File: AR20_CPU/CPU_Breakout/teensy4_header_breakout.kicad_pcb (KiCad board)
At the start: 4 copper layers, 65 x 77 mm, 80 parts, among them SW1 SW_SPST, U2 MCP1700_SOT23

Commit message: E
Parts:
- C11: value 100u -> .1u
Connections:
- net 25_A11 renamed 25_RX6_A11
- net 8_IN1 renamed 8_TX2_IN1
- CANmodule1 pad 1: 22_CTX1 -> 31_CTX3
- CANmodule1 pad 4: 23_CRX1 -> 30_CRX3
- D9 pad 1: 24_A10 -> 26_A12
- MX1 pad 22: 24_A10 -> 24_TX6_A10
- MX1 pad 37: 31_CTX3 -> 21_RX5
- MX1 pad 39: 30_CRX3 -> 20_TX5
- MX1 pad 43: 26_A12 -> Ground
- OpAmp1 pad 3: 24_A10 -> 26_A12
- OpAmp1 pad 4: 24_A10 -> 26_A12
- Teensy4.0 pad 10: 22_CTX1 -> Out1
- Teensy4.0 pad 12: Out2 -> 21_RX5
- Teensy4.0 pad 14: Out1 -> 20_TX5
- Teensy4.0 pad 38: 24_A10 -> 24_TX6_A10
- Teensy4.0 pad 8: 23_CRX1 -> Out2
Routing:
- net 24_A10: track 66.8 -> 0.00 mm, vias 2 -> 0
- net 23_CRX1: track 53.3 -> 0.00 mm, vias 1 -> 0
- net 24_TX6_A10: track 0.00 -> 49.8 mm
- net 22_CTX1: track 46.5 -> 0.00 mm, vias 1 -> 0
- net 20_TX5: track 0.00 -> 33.9 mm, vias 0 -> 2
- net 21_RX5: track 0.00 -> 27.8 mm, vias 0 -> 2
- net 31_CTX3: track 27.6 -> 17.6 mm, vias 0 -> 1
- net Out2: track 17.9 -> 15.9 mm
- net 26_A12: track 43.3 -> 41.5 mm, vias 0 -> 2
- net Out1: track 25.0 -> 23.2 mm
- net 30_CRX3: track 23.3 -> 21.5 mm, vias 0 -> 2
- net 12V_IN: track 71.4 -> 72.1 mm

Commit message: E2
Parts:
- removed C12: 0.1u, Capacitor_SMD:C_0603_1608Metric
- removed C13: 1u, Capacitor_SMD:C_0603_1608Metric
- removed JP11, JP12: SolderJumper_2_Open, Jumper:SolderJumper-2_P1.3mm_Open_RoundedPad1.0x1.5mm
- removed U2: MCP1700_SOT23, Package_TO_SOT_SMD:SOT-23
- moved JP10 5.95 mm to (129.7, 88.1), turned to 0 degrees
- moved R21 2.53 mm to (130.4, 90.3), turned to 0 degrees
- moved R22 2.45 mm to (130.4, 92.0), turned to 180 degrees
- moved C19 2.42 mm to (130.5, 94.0), turned to 180 degrees
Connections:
- C19 pad 1: Net-(C19-Pad1) -> IN+
- JP10 pad 1: IN+ -> Net-(JP10-Pad1)
- JP10 pad 2: Net-(C19-Pad1) -> VBAT
- MX1 pad 20: 3.3V -> Ground
- MX1 pad 21: 3V3 -> 3.3V
- R21 pad 1: VBAT -> Net-(JP10-Pad1)
- R21 pad 2: Net-(C19-Pad1) -> IN+
- R22 pad 1: Net-(C19-Pad1) -> IN+
- SDcard1 pad 4: Net-(JP11-Pad1) -> 3.3V
- Teensy4.0 pad 30: 3V3 -> 3.3V
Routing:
- net Net-(JP11-Pad1): track 25.3 -> 0.00 mm
- net 3V3: track 25.3 -> 0.00 mm
- net Net-(C19-Pad1): track 6.73 -> 0.00 mm
- net Vinn_5V: track 154.5 -> 148.2 mm
- net 3V3_OUT: track 5.73 -> 0.00 mm, vias 1 -> 0
- net IN+: track 5.58 -> 9.22 mm
- net Net-(JP10-Pad1): track 0.00 -> 3.30 mm
- net 3.3V: track 46.5 -> 45.0 mm, vias 1 -> 2
- added copper zone on Back_2_3V3, net 3.3V
- removed copper zone on Back_2_3V3, net 3V3_OUT

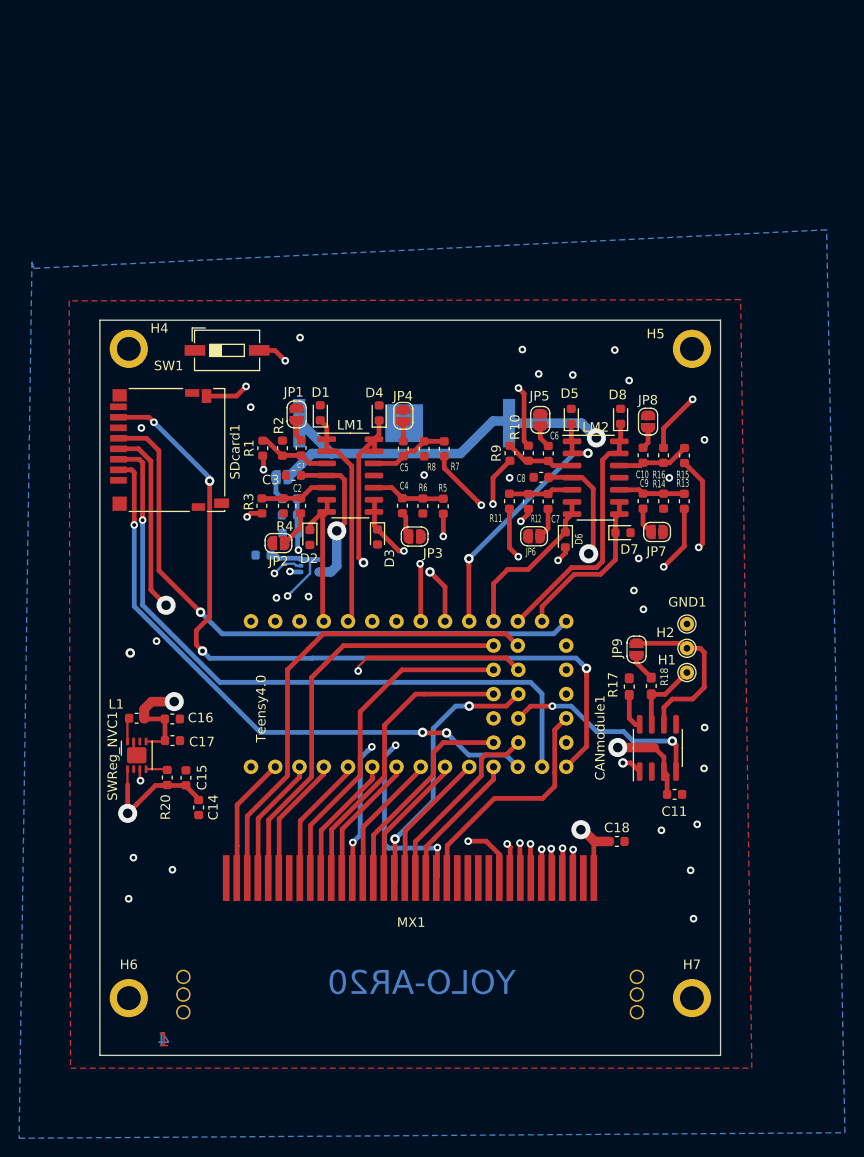
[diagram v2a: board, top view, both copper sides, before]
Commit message: Fixed push button
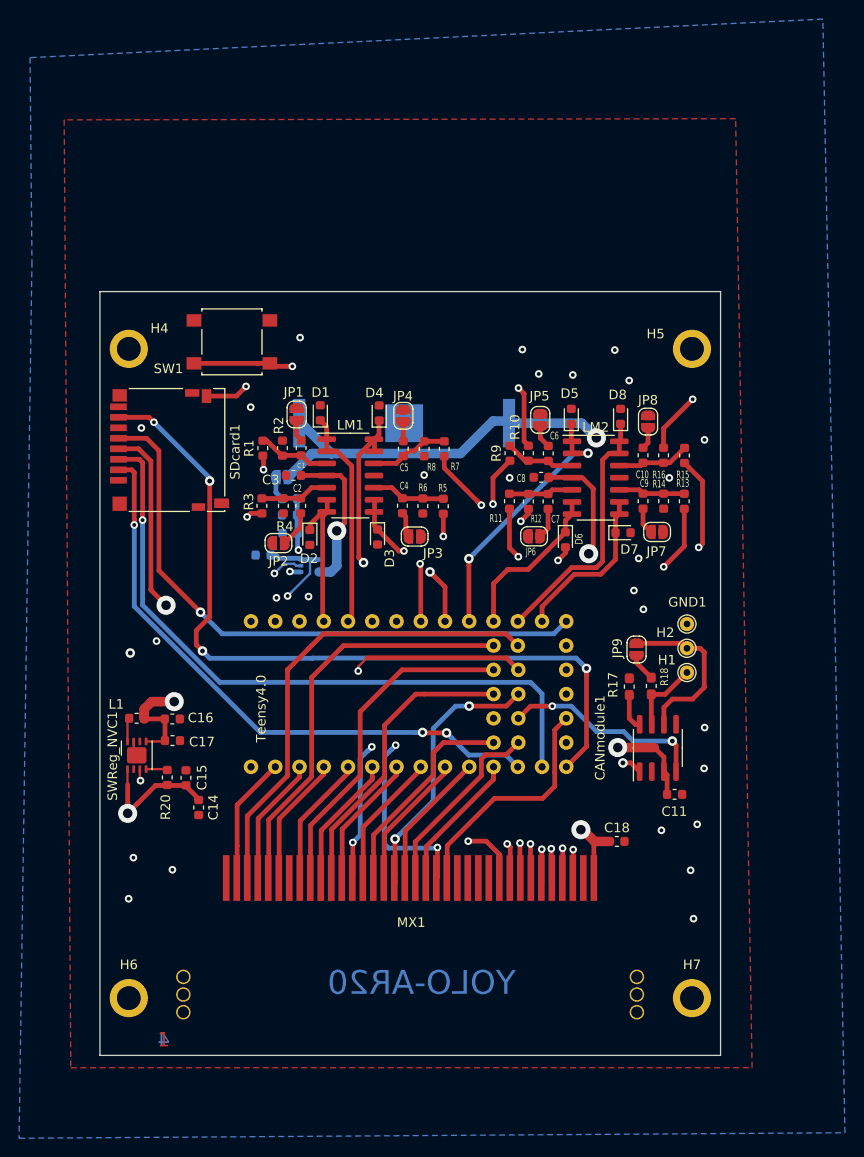
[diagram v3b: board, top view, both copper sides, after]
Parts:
- SW1: value SW_SPST -> SW_Push_Dual; footprint Button_Switch_SMD:SW_DIP_SPSTx01_Slide_6.7x4.1mm_W6.73mm_P2.54mm_LowProfile_JPin -> Button_Switch_SMD:SW_SPST_B3S-1000
- moved SW1 1.03 mm to (124.4, 73.9)
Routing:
- net ON_OFF: track 59.7 -> 66.0 mm
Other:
- board size 65 x 77 mm -> 65 x 80 mm

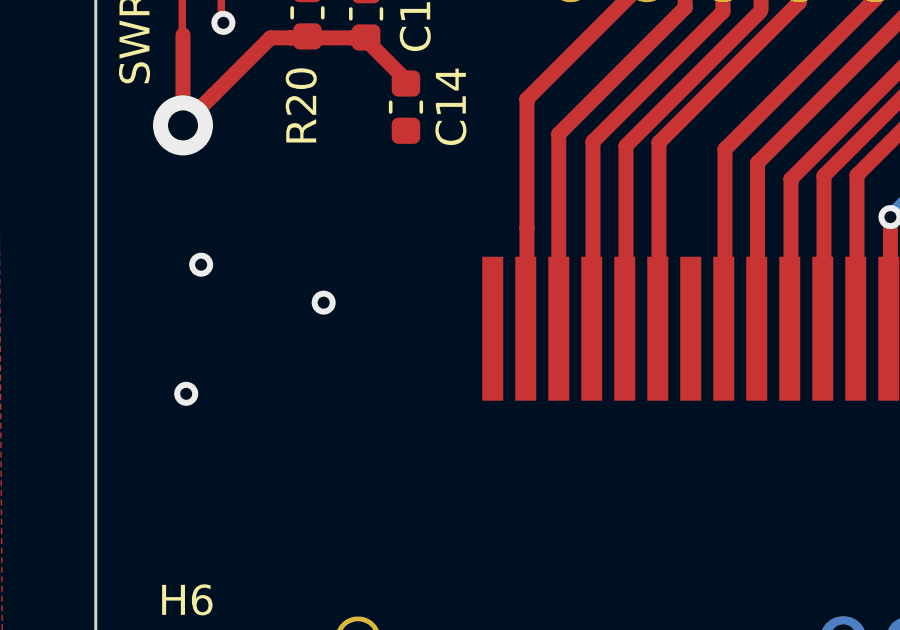
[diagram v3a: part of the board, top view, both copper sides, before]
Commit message: Added 5V pin
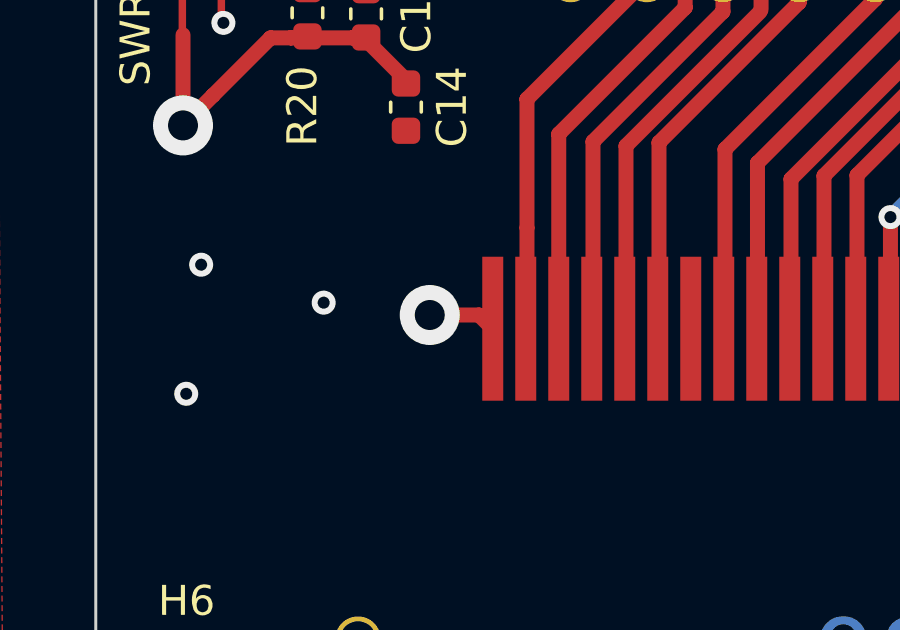
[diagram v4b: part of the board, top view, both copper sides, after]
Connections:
- MX1 pad 20: Ground -> Vinn_5V
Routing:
- net Vinn_5V: track 148.2 -> 150.7 mm, vias 4 -> 5
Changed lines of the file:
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@@
     (thickness 1.6)
     (drawings 9)
-    (tracks 695)
+    (tracks 699)
     (zones 0)
     (modules 75)
@@
     (add_net "Net-(CANmodule1-Pad7)")
     (add_net "Net-(CANmodule1-Pad8)")
+    (add_net "Net-(IC1-Pad1)")
+    (add_net "Net-(IC1-Pad10)")
+    (add_net "Net-(IC1-Pad11)")
+    (add_net "Net-(IC1-Pad12)")
+    (add_net "Net-(IC1-Pad13)")
+    (add_net "Net-(IC1-Pad14)")
+    (add_net "Net-(IC1-Pad2)")
+    (add_net "Net-(IC1-Pad3)")
+    (add_net "Net-(IC1-Pad4)")
+    (add_net "Net-(IC1-Pad5)")
+    (add_net "Net-(IC1-Pad6)")
+    (add_net "Net-(IC1-Pad7)")
+    (add_net "Net-(IC1-Pad8)")
+    (add_net "Net-(IC1-Pad9)")
     (add_net "Net-(JP10-Pad1)")
     (add_net "Net-(JP9-Pad1)")
@@
     (pad 60 thru_hole circle (at -23.75 -0.23642) (size 1.524 1.524) (drill 1.2) (layers *.Cu *.Mask))
     (pad 20 smd rect (at -19.25828 -10.58926) (size 0.7 4.8) (layers Front_GND F.Paste F.Mask)
-      (net 1 Ground))
+      (net 4 Vinn_5V))
     (pad 1 smd rect (at -18.15828 -10.58926) (size 0.7 4.8) (layers Front_GND F.Paste F.Mask)
       (net 34 0_RX1))
@@
   (segment (start 114.10454 116.88838) (end 114.42954 117.21338) (width 0.25) (layer Front_GND) (net 1))
   (segment (start 114.10454 115.76338) (end 114.10454 116.88838) (width 0.25) (layer Front_GND) (net 1))
-  (segment (start 123.8258 130.51616) (end 123.84278 130.53314) (width 0.5) (layer Front_GND) (net 1))
+  (via (at 121.70156 129.61112) (size 2) (drill 1) (layers Front_GND Back_GND) (net 4))
+  (segment (start 123.8258 130.51616) (end 123.84278 130.53314) (width 0.5) (layer Front_GND) (net 4))
   (segment (start 151.75 82.2) (end 148.34438 85.60562) (width 1) (layer Back_GND) (net 2))
   (segment (start 153.385 82.2) (end 151.75 82.2) (width 1) (layer Back_GND) (net 2))
@@
   (segment (start 115.9891 111.58982) (end 116.939627 111.58982) (width 1) (layer Front_GND) (net 4))
   (segment (start 115.20678 112.3569) (end 115.20678 112.37214) (width 0.5) (layer Front_GND) (net 4))
+  (segment (start 123.67768 129.94438) (end 123.80162 130.06832) (width 0.5) (layer Front_GND) (net 4))
+  (segment (start 123.34442 129.61112) (end 123.80162 130.06832) (width 0.5) (layer Front_GND) (net 4))
+  (segment (start 121.70156 129.61112) (end 123.34442 129.61112) (width 0.5) (layer Front_GND) (net 4))
   (via (at 121.113209 102.22507) (size 1) (drill 0.5) (layers Front_GND Back_GND) (net 5))
   (segment (start 123.376138 104.487999) (end 158.109901 104.487999) (width 0.5) (layer Back_GND) (net 5))

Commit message: Edit pads
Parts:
- GND1, H1, H2: footprint TestPoint:TestPoint_THTPad_D1.5mm_Drill0.7mm -> TestPoint:TestPoint_THTPad_D2.0mm_Drill1.0mm
- moved GND1 1.37 mm to (172.2, 102.1)
- moved H2 0.62 mm to (172.2, 105.4)
- moved Teensy4.0 0.20 mm to (126.6, 118.4)
- moved H1 0.10 mm to (172.2, 108.5)
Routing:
- net Net-(CANmodule1-Pad6): track 18.0 -> 18.7 mm

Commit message: Edit pads and traces
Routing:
- net VBAT: track 74.2 -> 75.1 mm
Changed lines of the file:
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@@
   (page A4)
   (layers
-    (0 Front_GND signal hide)
-    (1 Front_2_5V signal hide)
+    (0 Front_GND signal)
+    (1 Front_2_5V signal)
     (2 Back_2_3V3 signal)
-    (31 Back_GND signal hide)
+    (31 Back_GND signal)
     (32 B.Adhes user)
     (33 F.Adhes user)
@@
   (segment (start 148.34438 85.60562) (end 135.88746 85.60562) (width 1) (layer Back_GND) (net 2))
   (via (at 162.57016 83.9724) (size 2) (drill 1) (layers Front_GND Back_GND) (net 2))
-  (segment (start 163.570159 111.709841) (end 159.42 115.86) (width 1) (layer Back_2_3V3) (net 2))
-  (segment (start 162.57016 83.9724) (end 163.570159 84.972399) (width 1) (layer Back_2_3V3) (net 2))
-  (segment (start 163.570159 84.972399) (end 163.570159 111.709841) (width 1) (layer Back_2_3V3) (net 2))
   (segment (start 161.570161 82.972401) (end 162.57016 83.9724) (width 1) (layer Back_GND) (net 2))
   (segment (start 153.42058 82.42808) (end 161.02584 82.42808) (width 1) (layer Back_GND) (net 2))
@@
   (segment (start 132.77342 85.60562) (end 130.302 88.07704) (width 1) (layer Back_GND) (net 2))
   (segment (start 134.82062 85.60562) (end 132.77342 85.60562) (width 1) (layer Back_GND) (net 2))
+  (segment (start 164.65042 110.62958) (end 159.42 115.86) (width 1) (layer Back_2_3V3) (net 2))
+  (segment (start 162.57016 83.9724) (end 164.65042 86.05266) (width 1) (layer Back_2_3V3) (net 2))
+  (segment (start 164.65042 86.05266) (end 164.65042 110.62958) (width 1) (layer Back_2_3V3) (net 2))
   (via (at 132.42036 100.58908) (size 0.8) (drill 0.4) (layers Front_GND Back_GND) (net 3))
   (via (at 130.72618 76.4794) (size 0.8) (drill 0.4) (layers Front_GND Back_GND) (net 3))

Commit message: Gerber file 1.0 generated
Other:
- board text added: "T4.0AR20"
- board text removed: "YOLO-AR20"
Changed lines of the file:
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@@
     (effects (font (size 1.5 1.5) (thickness 0.3)))
   )
-  (gr_text YOLO-AR20 (at 144.26184 141.04112) (layer Back_GND)
+  (gr_text T4.0AR20 (at 144.26184 141.04112) (layer Back_GND)
     (effects (font (size 2.5 2.5) (thickness 0.625)) (justify mirror))
   )

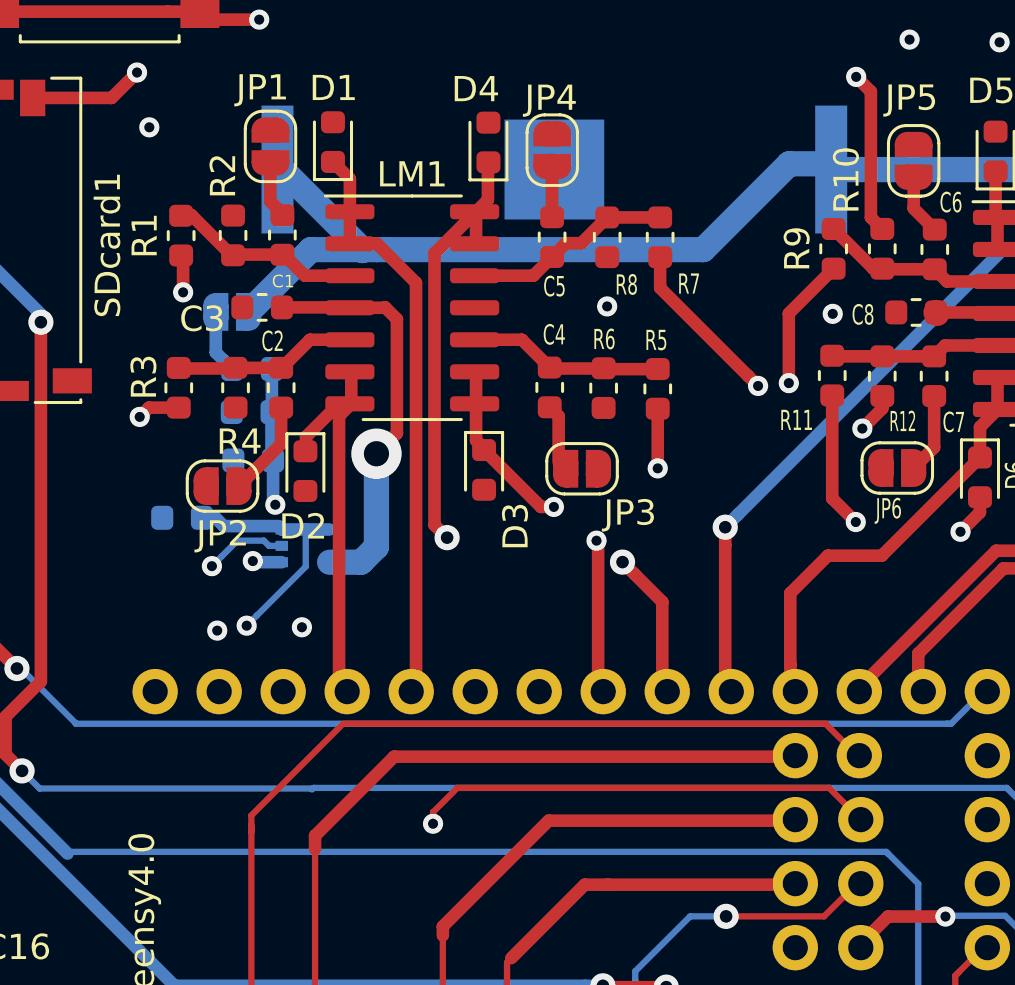
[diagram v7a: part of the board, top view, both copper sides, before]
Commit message: V2.0 Teensy Breakout Board
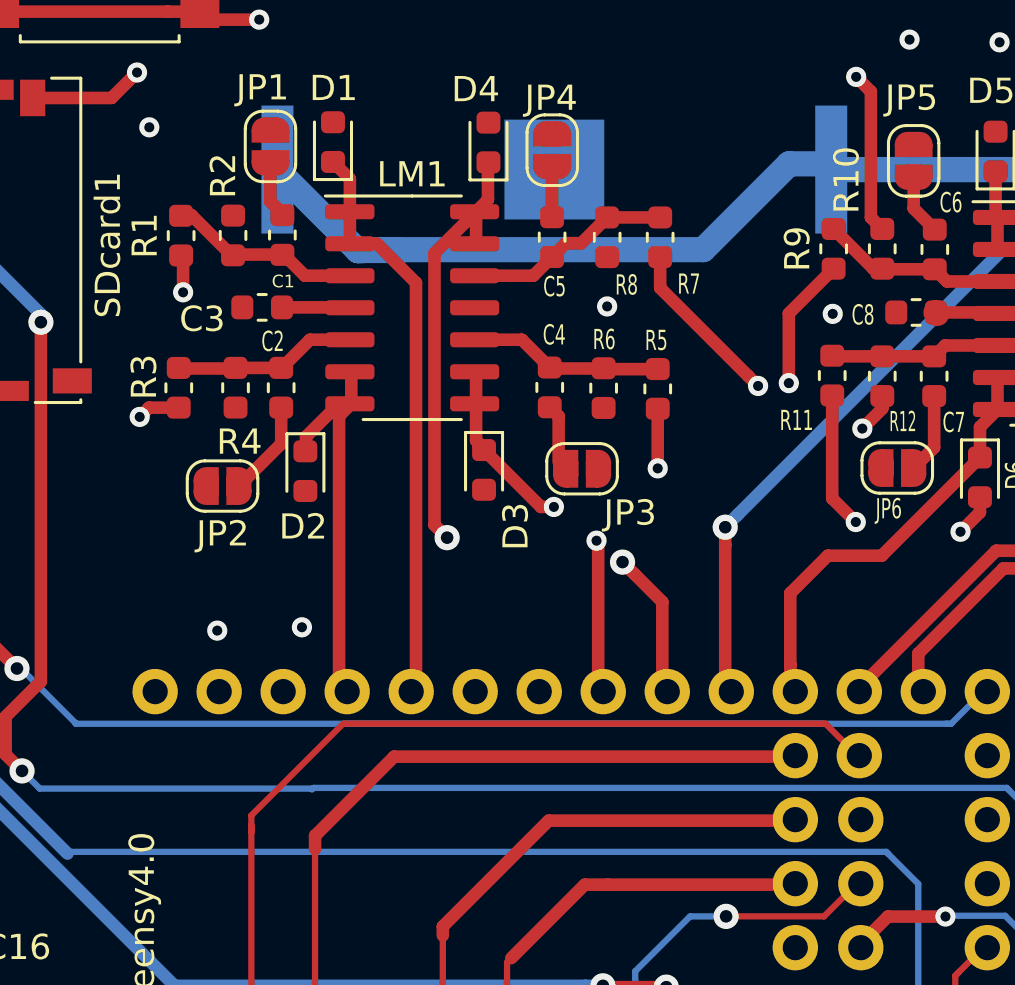
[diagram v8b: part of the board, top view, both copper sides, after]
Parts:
- removed C19: ?, Capacitor_SMD:C_0603_1608Metric
- removed D9: 3V, Diode_SMD:D_0603_1608Metric
- removed JP10: SolderJumper_2_Open, Jumper:SolderJumper-2_P1.3mm_Open_RoundedPad1.0x1.5mm
- removed OpAmp1: NCV20091SQ3T2G, Teensy_Footprint_Library:SC−70_NCV20091SQ3T2G
- removed R21, R22: ?, Resistor_SMD:R_0603_1608Metric
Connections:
- Teensy4.0 pad 37: 26_A12 -> (no net)
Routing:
- net 26_A12: track 41.7 -> 0.00 mm, vias 2 -> 0
- net Vinn_5V: track 150.7 -> 113.3 mm, vias 5 -> 4
- net IN+: track 9.22 -> 0.00 mm, vias 2 -> 0
- net Net-(JP10-Pad1): track 3.30 -> 0.00 mm
- net Ground: track 27.6 -> 24.4 mm, vias 33 -> 32
- net VBAT: track 75.1 -> 72.0 mm
